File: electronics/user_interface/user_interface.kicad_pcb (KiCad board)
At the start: 2 copper layers, 80 x 80 mm, 87 parts, among them J1 Conn_01x06, J2 Conn_02x05_Odd_Even, SW1 ALPS_EC11E18244A5, U1 PCF8574, U2 PCF8574

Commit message: some routing
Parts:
- moved C2 2.60 mm to (140.7, 93.1)
- moved U1 2.60 mm to (140.6, 86.3)
- moved R25 2.60 mm to (148.4, 85.7)
- moved R5 2.60 mm to (132.8, 91.0), turned to 180 degrees
- moved R6 2.60 mm to (132.8, 89.5), turned to 180 degrees
- moved R7 2.60 mm to (132.8, 88.0), turned to 180 degrees
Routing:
- net /VDD_BACKLIGHT: track 2.76 -> 69.0 mm, vias 0 -> 2
- net /VDD: track 40.9 -> 65.1 mm, vias 1 -> 3
- net /VSS: track 44.7 -> 48.9 mm, vias 4 -> 5
- net Net-(R7-Pad1): track 0.00 -> 2.68 mm
- net Net-(R5-Pad1): track 0.00 -> 2.66 mm
- net Net-(R6-Pad1): track 0.00 -> 2.59 mm

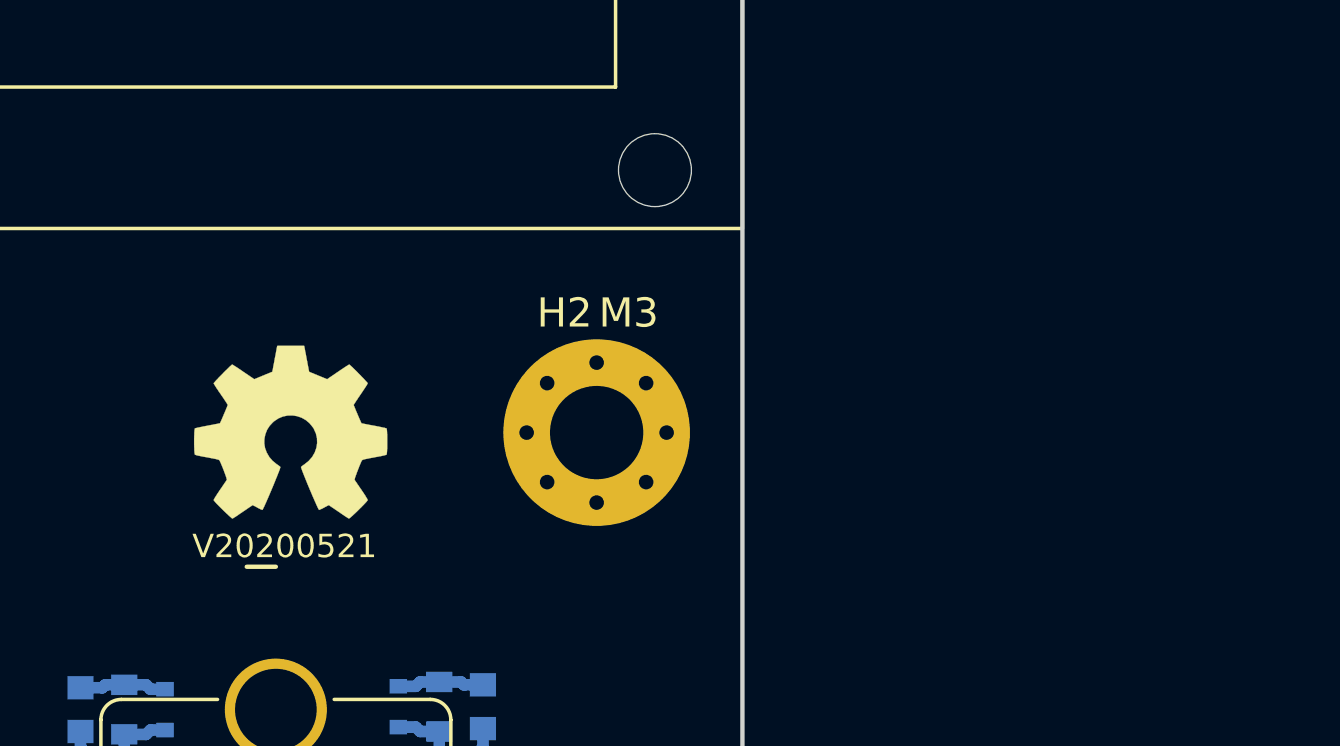
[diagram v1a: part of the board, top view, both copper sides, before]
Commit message: added pullup resistors, updated versionnumber
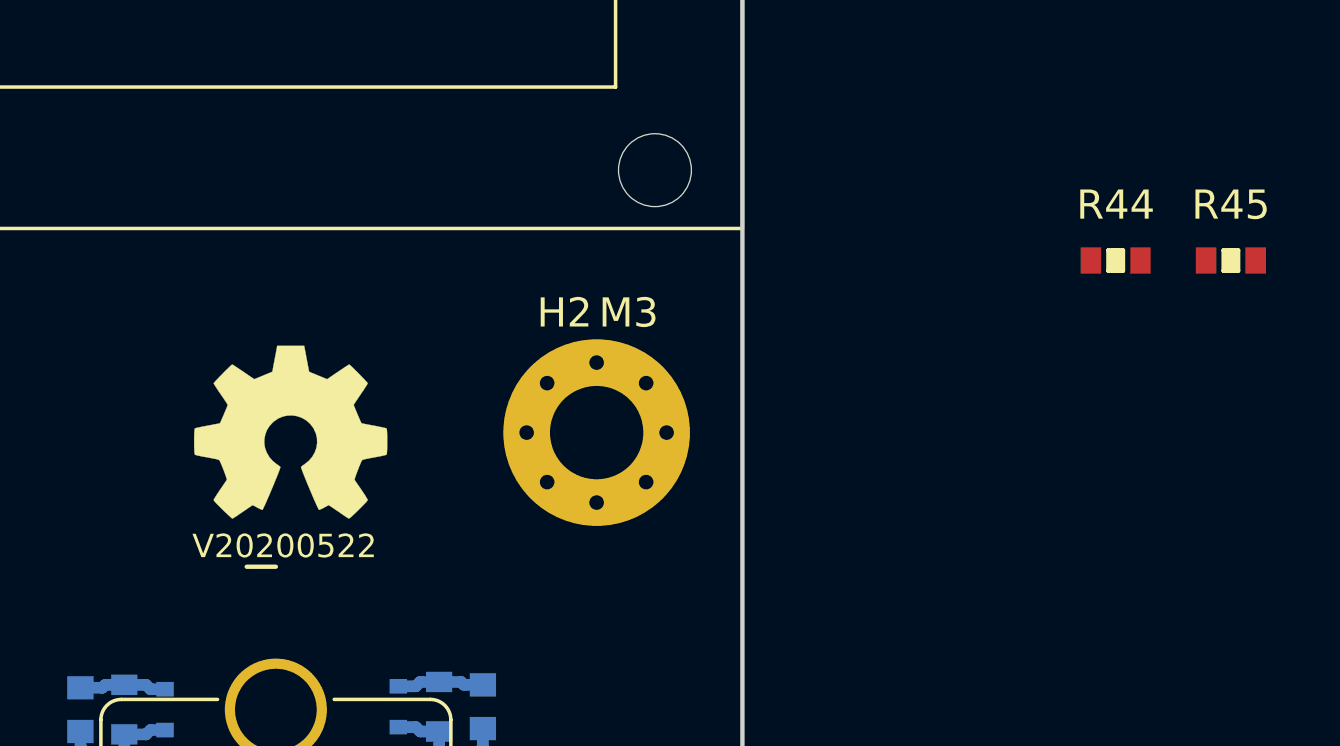
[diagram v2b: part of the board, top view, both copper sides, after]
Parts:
- added R44: 4.7K, SquantorRcl:R_0603_hand, F.Cu at (202.8, 109.1)
- added R45: 4.7K, SquantorRcl:R_0603_hand, F.Cu at (206.8, 109.1)
- N2: value V20200521 -> V20200522
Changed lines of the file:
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@@
     (tracks 270)
     (zones 0)
-    (modules 87)
+    (modules 89)
     (nets 48)
   )
@@
     (add_net "Net-(R9-Pad1)")
   )
+  (module SquantorRcl:R_0603_hand (layer F.Cu)
+    (at 206.75 109.1)
+    (descr "Resistor SMD 0603, reflow soldering, Vishay (see dcrcw.pdf)")
+    (tags "resistor 0603")
+    (attr smd)
+    (fp_text reference R45 (at 0 -1.9) (layer F.SilkS)
+      (effects (font (size 1 1) (thickness 0.15)))
+    )
+    (fp_text value 4.7K (at 0 1.9) (layer F.Fab)
+      (effects (font (size 1 1) (thickness 0.15)))
+    )
+    (fp_line (start -0.8 0.4) (end -0.8 -0.4) (layer F.Fab) (width 0.1))
+    (fp_line (start 0.8 0.4) (end -0.8 0.4) (layer F.Fab) (width 0.1))
+    (fp_line (start 0.8 -0.4) (end 0.8 0.4) (layer F.Fab) (width 0.1))
+    (fp_line (start -0.8 -0.4) (end 0.8 -0.4) (layer F.Fab) (width 0.1))
+    (fp_line (start -1.45 -0.75) (end 1.45 -0.75) (layer F.CrtYd) (width 0.05))
+    (fp_line (start -1.45 0.75) (end 1.45 0.75) (layer F.CrtYd) (width 0.05))
+    (fp_line (start -1.45 -0.75) (end -1.45 0.75) (layer F.CrtYd) (width 0.05))
+    (fp_line (start 1.45 -0.75) (end 1.45 0.75) (layer F.CrtYd) (width 0.05))
+    (fp_line (start 0.25 -0.35) (end 0.25 0.35) (layer F.SilkS) (width 0.15))
+    (fp_line (start -0.25 0.35) (end -0.25 -0.35) (layer F.SilkS) (width 0.15))
+    (fp_line (start -0.25 -0.35) (end 0.25 -0.35) (layer F.SilkS) (width 0.15))
+    (fp_line (start 0.25 0.35) (end -0.25 0.35) (layer F.SilkS) (width 0.15))
+    (fp_line (start -0.1 0.35) (end -0.1 -0.35) (layer F.SilkS) (width 0.15))
+    (fp_line (start -0.1 -0.35) (end 0.1 -0.35) (layer F.SilkS) (width 0.15))
+    (fp_line (start 0.1 -0.35) (end 0.1 0.35) (layer F.SilkS) (width 0.15))
+    (fp_line (start 0 0.35) (end 0 -0.35) (layer F.SilkS) (width 0.15))
+    (pad 2 smd rect (at 0.85 0) (size 0.7 0.9) (layers F.Cu F.Paste F.Mask)
+      (net 2 /VDD))
+    (pad 1 smd rect (at -0.85 0) (size 0.7 0.9) (layers F.Cu F.Paste F.Mask)
+      (net 5 /SCL))
+    (model ${KISYS3DMOD}/Resistor_SMD.3dshapes/R_0603_1608Metric.step
+      (at (xyz 0 0 0))
+      (scale (xyz 1 1 1))
+      (rotate (xyz 0 0 0))
+    )
+  )
+  (module SquantorRcl:R_0603_hand (layer F.Cu)
+    (at 202.8 109.1)
+    (descr "Resistor SMD 0603, reflow soldering, Vishay (see dcrcw.pdf)")
+    (tags "resistor 0603")
+    (attr smd)
+    (fp_text reference R44 (at 0 -1.9) (layer F.SilkS)
+      (effects (font (size 1 1) (thickness 0.15)))
+    )
+    (fp_text value 4.7K (at 0 1.9) (layer F.Fab)
+      (effects (font (size 1 1) (thickness 0.15)))
+    )
+    (fp_line (start -0.8 0.4) (end -0.8 -0.4) (layer F.Fab) (width 0.1))
+    (fp_line (start 0.8 0.4) (end -0.8 0.4) (layer F.Fab) (width 0.1))
+    (fp_line (start 0.8 -0.4) (end 0.8 0.4) (layer F.Fab) (width 0.1))
+    (fp_line (start -0.8 -0.4) (end 0.8 -0.4) (layer F.Fab) (width 0.1))
+    (fp_line (start -1.45 -0.75) (end 1.45 -0.75) (layer F.CrtYd) (width 0.05))
+    (fp_line (start -1.45 0.75) (end 1.45 0.75) (layer F.CrtYd) (width 0.05))
+    (fp_line (start -1.45 -0.75) (end -1.45 0.75) (layer F.CrtYd) (width 0.05))
+    (fp_line (start 1.45 -0.75) (end 1.45 0.75) (layer F.CrtYd) (width 0.05))
+    (fp_line (start 0.25 -0.35) (end 0.25 0.35) (layer F.SilkS) (width 0.15))
+    (fp_line (start -0.25 0.35) (end -0.25 -0.35) (layer F.SilkS) (width 0.15))
+    (fp_line (start -0.25 -0.35) (end 0.25 -0.35) (layer F.SilkS) (width 0.15))
+    (fp_line (start 0.25 0.35) (end -0.25 0.35) (layer F.SilkS) (width 0.15))
+    (fp_line (start -0.1 0.35) (end -0.1 -0.35) (layer F.SilkS) (width 0.15))
+    (fp_line (start -0.1 -0.35) (end 0.1 -0.35) (layer F.SilkS) (width 0.15))
+    (fp_line (start 0.1 -0.35) (end 0.1 0.35) (layer F.SilkS) (width 0.15))
+    (fp_line (start 0 0.35) (end 0 -0.35) (layer F.SilkS) (width 0.15))
+    (pad 2 smd rect (at 0.85 0) (size 0.7 0.9) (layers F.Cu F.Paste F.Mask)
+      (net 2 /VDD))
+    (pad 1 smd rect (at -0.85 0) (size 0.7 0.9) (layers F.Cu F.Paste F.Mask)
+      (net 6 /SDA))
+    (model ${KISYS3DMOD}/Resistor_SMD.3dshapes/R_0603_1608Metric.step
+      (at (xyz 0 0 0))
+      (scale (xyz 1 1 1))
+      (rotate (xyz 0 0 0))
+    )
+  )
   (module Symbol:OSHW-Symbol_6.7x6mm_SilkScreen (layer F.Cu)
     (at 174.5 115)
@@
       (effects (font (size 1 1) (thickness 0.15)))
     )
-    (fp_text value V20200521 (at 0.8 -0.1) (layer F.SilkS)
+    (fp_text value V20200522 (at 0.8 -0.1) (layer F.SilkS)
       (effects (font (size 0.8 0.8) (thickness 0.15)))
     )

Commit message: routing completed
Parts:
- added R46: 4.7K, SquantorRcl:R_0603_hand, B.Cu at (157.9, 88.9)
- R44, R45: moved to B.Cu
- moved R45 53.5 mm to (157.9, 87.4), turned to 180 degrees
- moved R44 50.5 mm to (157.9, 85.9), turned to 180 degrees
- moved C3 2.30 mm to (166.4, 82.6), turned to 0 degrees
- moved R10 1.57 mm to (174.0, 87.6), turned to 0 degrees
- moved R8 1.43 mm to (174.0, 84.6), turned to 0 degrees
- moved R9 1.41 mm to (174.0, 86.1), turned to 0 degrees
- moved R26 0.75 mm to (157.9, 93.8)
- moved C2 0.10 mm to (140.7, 93.0)
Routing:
- net /VDD: track 65.1 -> 374.8 mm, vias 3 -> 7
- net /Button_01: track 5.51 -> 95.8 mm
- net /Button_00: track 5.51 -> 74.9 mm
- net /Rotary_A_filtered: track 3.00 -> 61.2 mm, vias 0 -> 2
- net /Button_03: track 5.51 -> 57.4 mm
- net /!INT: track 2.00 -> 51.6 mm, vias 0 -> 3
- net /SDA: track 0.00 -> 46.3 mm, vias 0 -> 3
- net /SCL: track 0.00 -> 42.7 mm, vias 0 -> 3
- net /Rotary_B_filtered: track 3.00 -> 42.3 mm, vias 0 -> 2
- net /Rotary_push_filtered: track 3.00 -> 40.8 mm, vias 0 -> 2
- net /Button_02: track 5.51 -> 39.9 mm
- net /VSS: track 48.9 -> 74.6 mm, vias 5 -> 9
- net /RS: track 1.56 -> 25.7 mm, vias 0 -> 1
- net /RW: track 1.57 -> 23.4 mm, vias 0 -> 1
- net /E: track 1.55 -> 22.2 mm, vias 0 -> 1
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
